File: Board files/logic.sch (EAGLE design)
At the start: 21 parts, among them U1 LD1117, U2 LM2662, U3 LD1085V

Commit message: Minor logic board changes
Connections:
- net 6V: now also R1.1; no longer R1.2
- net GND: now also R2.2; no longer R2.1
- net N$4: now also R1.2, R2.1; no longer R1.1, R2.2
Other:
- moved on the sheet: R1, R2
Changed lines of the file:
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@@
 <instance part="GND6" gate="1" x="137.16" y="91.44"/>
 <instance part="GND7" gate="1" x="177.8" y="91.44"/>
-<instance part="R1" gate="G$1" x="170.18" y="99.06" rot="R90"/>
-<instance part="R2" gate="G$1" x="152.4" y="83.82" rot="R90"/>
+<instance part="R1" gate="G$1" x="170.18" y="99.06" rot="R270"/>
+<instance part="R2" gate="G$1" x="152.4" y="83.82" rot="R270"/>
 <instance part="GND8" gate="1" x="152.4" y="73.66"/>
 <instance part="SUPPLY7" gate="G$1" x="137.16" y="45.72"/>
@@
 </segment>
 <segment>
-<pinref part="R2" gate="G$1" pin="1"/>
+<pinref part="R2" gate="G$1" pin="2"/>
 <pinref part="GND8" gate="1" pin="GND"/>
 <wire x1="152.4" y1="76.2" x2="152.4" y2="78.74" width="0.1524" layer="91"/>
@@
 <junction x="177.8" y="106.68"/>
 <label x="177.8" y="109.22" size="1.778" layer="95"/>
-<pinref part="R1" gate="G$1" pin="2"/>
+<pinref part="R1" gate="G$1" pin="1"/>
 <wire x1="170.18" y1="104.14" x2="170.18" y2="106.68" width="0.1524" layer="91"/>
 <junction x="170.18" y="106.68"/>
@@
 <segment>
 <pinref part="U3" gate="1" pin="ADJ"/>
-<pinref part="R2" gate="G$1" pin="2"/>
+<pinref part="R2" gate="G$1" pin="1"/>
 <wire x1="152.4" y1="99.06" x2="152.4" y2="91.44" width="0.1524" layer="91"/>
-<pinref part="R1" gate="G$1" pin="1"/>
+<pinref part="R1" gate="G$1" pin="2"/>
 <wire x1="152.4" y1="91.44" x2="152.4" y2="88.9" width="0.1524" layer="91"/>
 <wire x1="170.18" y1="93.98" x2="170.18" y2="91.44" width="0.1524" layer="91"/>

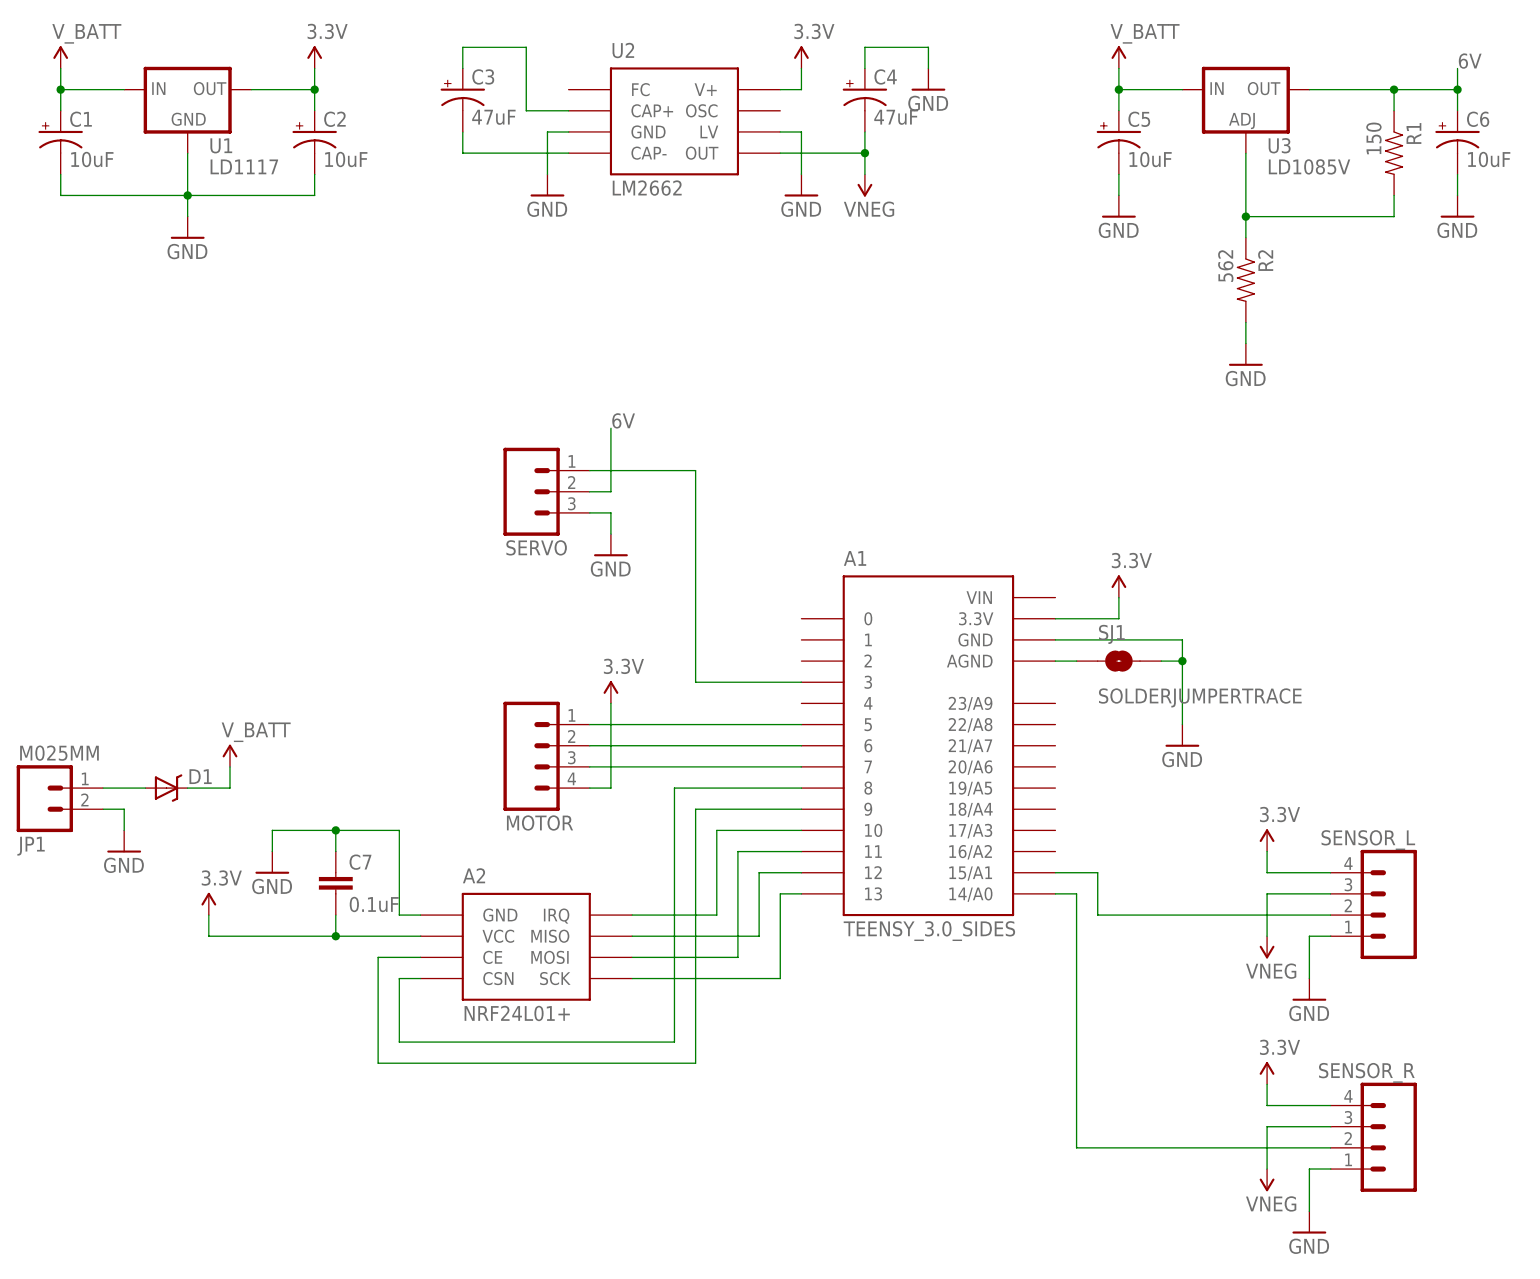
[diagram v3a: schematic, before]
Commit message: Switched to polarized connectors
Also added 3.3v out pins on logic board, various other changes
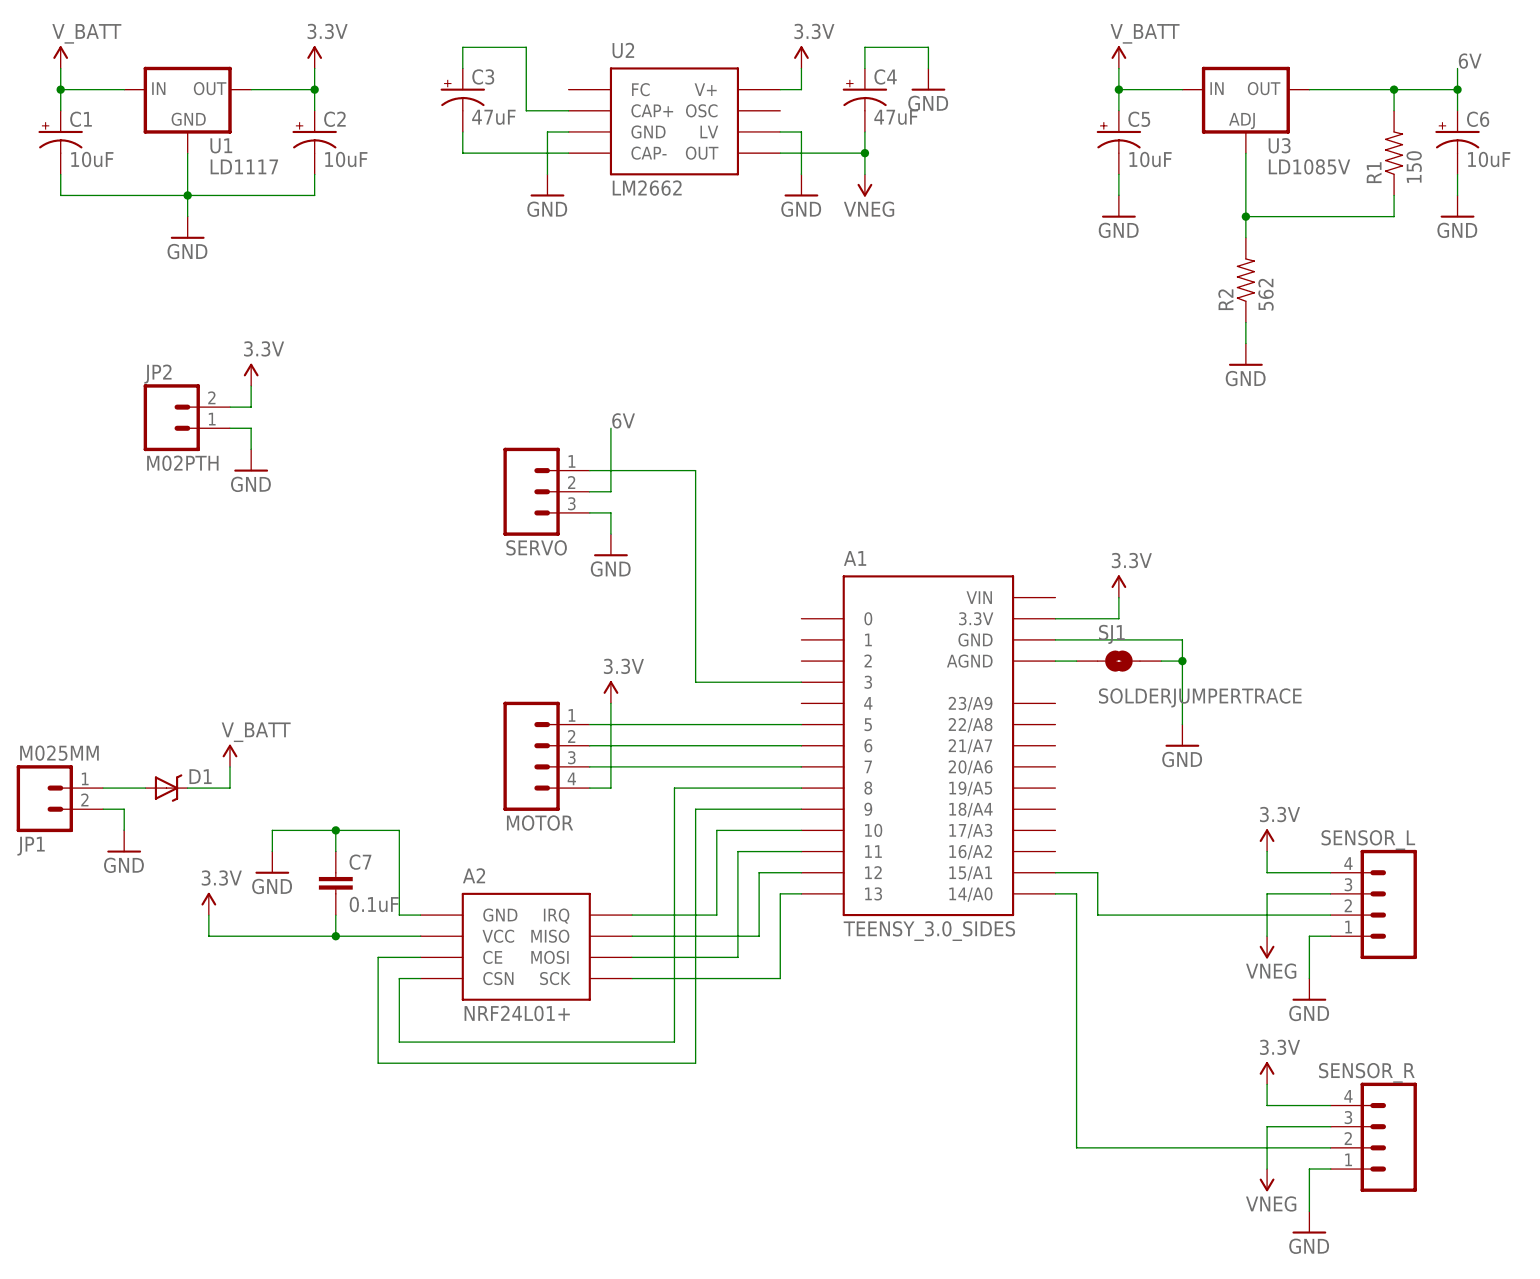
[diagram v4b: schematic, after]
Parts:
- added JP2: M02PTH, SparkFun-Connectors:M02PTH
- MOTOR, SENSOR_L, SENSOR_R: device SparkFun-Connectors:M04LOCK -> SparkFun-Connectors:M04POLAR_LOCK
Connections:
- net 3.3V: now also JP2.2
- net 6V: now also R1.2; no longer R1.1
- net GND: now also JP2.1, R2.1; no longer R2.2
- net N$4: now also R1.1, R2.2; no longer R1.2, R2.1
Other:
- moved on the sheet: R1, R2
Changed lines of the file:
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@@
 <part name="A1" library="Teensy3.0" deviceset="TEENSY_3.0_SIDES" device=""/>
 <part name="SERVO" library="SparkFun-Connectors" deviceset="M03" device="LOCK_LONGPADS"/>
-<part name="SENSOR_L" library="SparkFun-Connectors" deviceset="M04" device="LOCK"/>
-<part name="SENSOR_R" library="SparkFun-Connectors" deviceset="M04" device="LOCK"/>
+<part name="SENSOR_L" library="SparkFun-Connectors" deviceset="M04" device="POLAR_LOCK"/>
+<part name="SENSOR_R" library="SparkFun-Connectors" deviceset="M04" device="POLAR_LOCK"/>
 <part name="GND10" library="SparkFun-Aesthetics" deviceset="GND" device=""/>
 <part name="SUPPLY8" library="SparkFun-Aesthetics" deviceset="3.3V" device=""/>
@@
 <part name="SUPPLY13" library="SparkFun-Aesthetics" deviceset="3.3V" device=""/>
 <part name="C7" library="SparkFun-Capacitors" deviceset="CAP" device="0805" value="0.1uF"/>
-<part name="MOTOR" library="SparkFun-Connectors" deviceset="M04" device="LOCK"/>
+<part name="MOTOR" library="SparkFun-Connectors" deviceset="M04" device="POLAR_LOCK"/>
 <part name="GND11" library="SparkFun-Aesthetics" deviceset="GND" device=""/>
 <part name="GND12" library="SparkFun-Aesthetics" deviceset="GND" device=""/>
 <part name="SJ1" library="SparkFun-Passives" deviceset="SOLDERJUMPER" device="TRACE"/>
+<part name="JP2" library="SparkFun-Connectors" deviceset="M02" device="PTH"/>
+<part name="SUPPLY14" library="SparkFun-Aesthetics" deviceset="3.3V" device=""/>
+<part name="GND14" library="SparkFun-Aesthetics" deviceset="GND" device=""/>
 </parts>
 <sheets>
@@
 <instance part="GND6" gate="1" x="137.16" y="91.44"/>
 <instance part="GND7" gate="1" x="177.8" y="91.44"/>
-<instance part="R1" gate="G$1" x="170.18" y="99.06" rot="R270"/>
-<instance part="R2" gate="G$1" x="152.4" y="83.82" rot="R270"/>
+<instance part="R1" gate="G$1" x="170.18" y="99.06" rot="R90"/>
+<instance part="R2" gate="G$1" x="152.4" y="83.82" rot="R90"/>
 <instance part="GND8" gate="1" x="152.4" y="73.66"/>
 <instance part="SUPPLY7" gate="G$1" x="137.16" y="45.72"/>
@@
 <instance part="GND12" gate="1" x="160.02" y="-30.48"/>
 <instance part="SJ1" gate="1" x="137.16" y="38.1"/>
+<instance part="JP2" gate="G$1" x="22.86" y="66.04"/>
+<instance part="SUPPLY14" gate="G$1" x="33.02" y="71.12"/>
+<instance part="GND14" gate="1" x="33.02" y="60.96"/>
 </instances>
 <busses>
@@
 </segment>
 <segment>
-<pinref part="R2" gate="G$1" pin="2"/>
+<pinref part="R2" gate="G$1" pin="1"/>
 <pinref part="GND8" gate="1" pin="GND"/>
 <wire x1="152.4" y1="76.2" x2="152.4" y2="78.74" width="0.1524" layer="91"/>
@@
 <pinref part="GND12" gate="1" pin="GND"/>
 </segment>
+<segment>
+<pinref part="JP2" gate="G$1" pin="1"/>
+<pinref part="GND14" gate="1" pin="GND"/>
+<wire x1="30.48" y1="66.04" x2="33.02" y2="66.04" width="0.1524" layer="91"/>
+<wire x1="33.02" y1="66.04" x2="33.02" y2="63.5" width="0.1524" layer="91"/>
+</segment>
 </net>
 <net name="V_BATT" class="0">
@@
 <junction x="43.18" y="5.08"/>
 </segment>
+<segment>
+<pinref part="JP2" gate="G$1" pin="2"/>
+<pinref part="SUPPLY14" gate="G$1" pin="3.3V"/>
+<wire x1="30.48" y1="68.58" x2="33.02" y2="68.58" width="0.1524" layer="91"/>
+<wire x1="33.02" y1="68.58" x2="33.02" y2="71.12" width="0.1524" layer="91"/>
+</segment>
 </net>
 <net name="VNEG" class="0">
@@
 <junction x="177.8" y="106.68"/>
 <label x="177.8" y="109.22" size="1.778" layer="95"/>
-<pinref part="R1" gate="G$1" pin="1"/>
+<pinref part="R1" gate="G$1" pin="2"/>
 <wire x1="170.18" y1="104.14" x2="170.18" y2="106.68" width="0.1524" layer="91"/>
 <junction x="170.18" y="106.68"/>
@@
 <segment>
 <pinref part="U3" gate="1" pin="ADJ"/>
-<pinref part="R2" gate="G$1" pin="1"/>
+<pinref part="R2" gate="G$1" pin="2"/>
 <wire x1="152.4" y1="99.06" x2="152.4" y2="91.44" width="0.1524" layer="91"/>
-<pinref part="R1" gate="G$1" pin="2"/>
+<pinref part="R1" gate="G$1" pin="1"/>
 <wire x1="152.4" y1="91.44" x2="152.4" y2="88.9" width="0.1524" layer="91"/>
 <wire x1="170.18" y1="93.98" x2="170.18" y2="91.44" width="0.1524" layer="91"/>
